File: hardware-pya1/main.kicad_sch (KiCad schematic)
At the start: 64 parts, among them J6 USB_C_Receptacle_USB2.0_16P, J7 Conn_02x08_Odd_Even, Q6 BSS138, SW1 SW_Push, SW10 SW_Push, SW11 SW_Push, SW12 SW_Push, SW13 SW_Push, SW14 SW_Push, SW15 SW_Push, SW16 SW_Push, SW17 SW_Push, SW18 SW_Push, SW19 SW_Push, SW2 SW_Push, SW20 SW_Push, SW21 Encoder, SW22 SW_Push, SW3 SW_Push, SW4 SW_Push, SW5 SW_Push, SW6 SW_Push, SW7 SW_Push, SW8 SW_Push, SW9 SW_Push, U3 74HC595, U4 ESP32-S3-WROOM-1

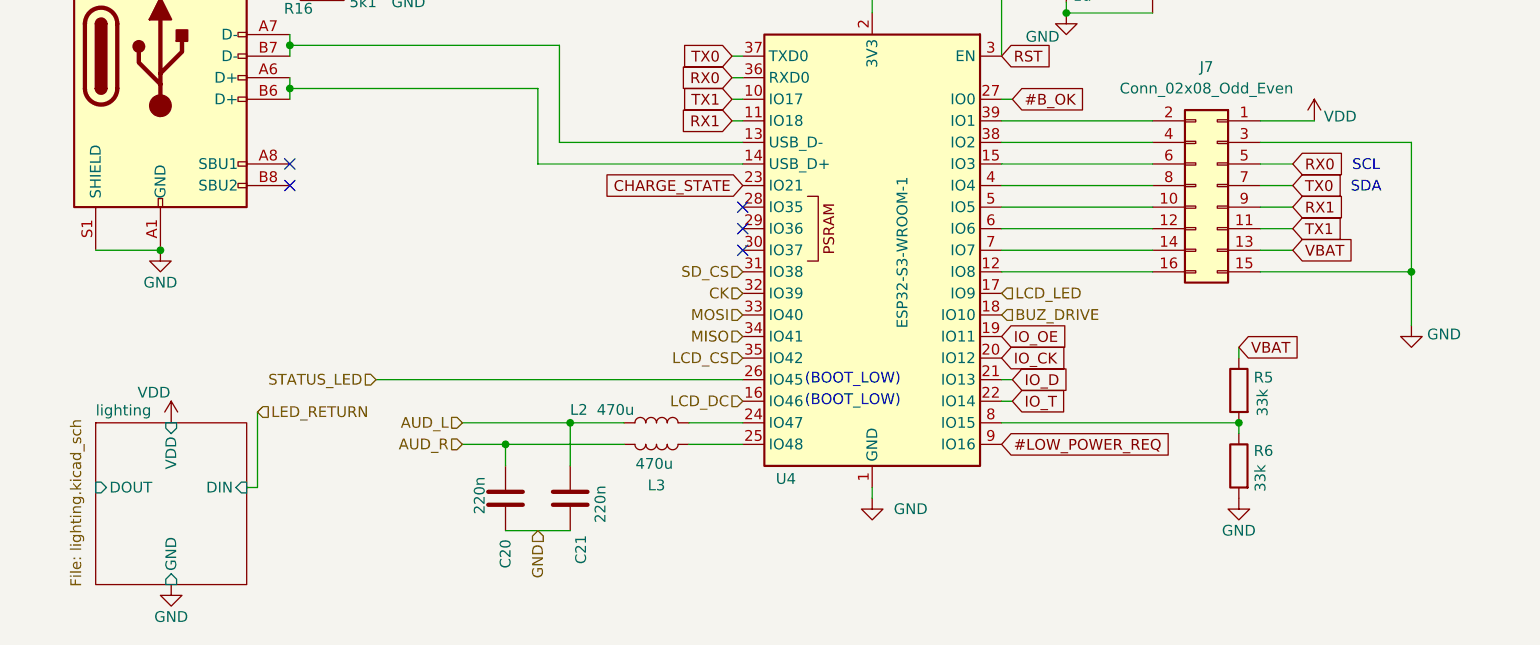
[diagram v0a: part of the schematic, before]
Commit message: pcb: redesign fix for LowPowerReq - added passives optional cap for slowstart on regulator switching to hi-power
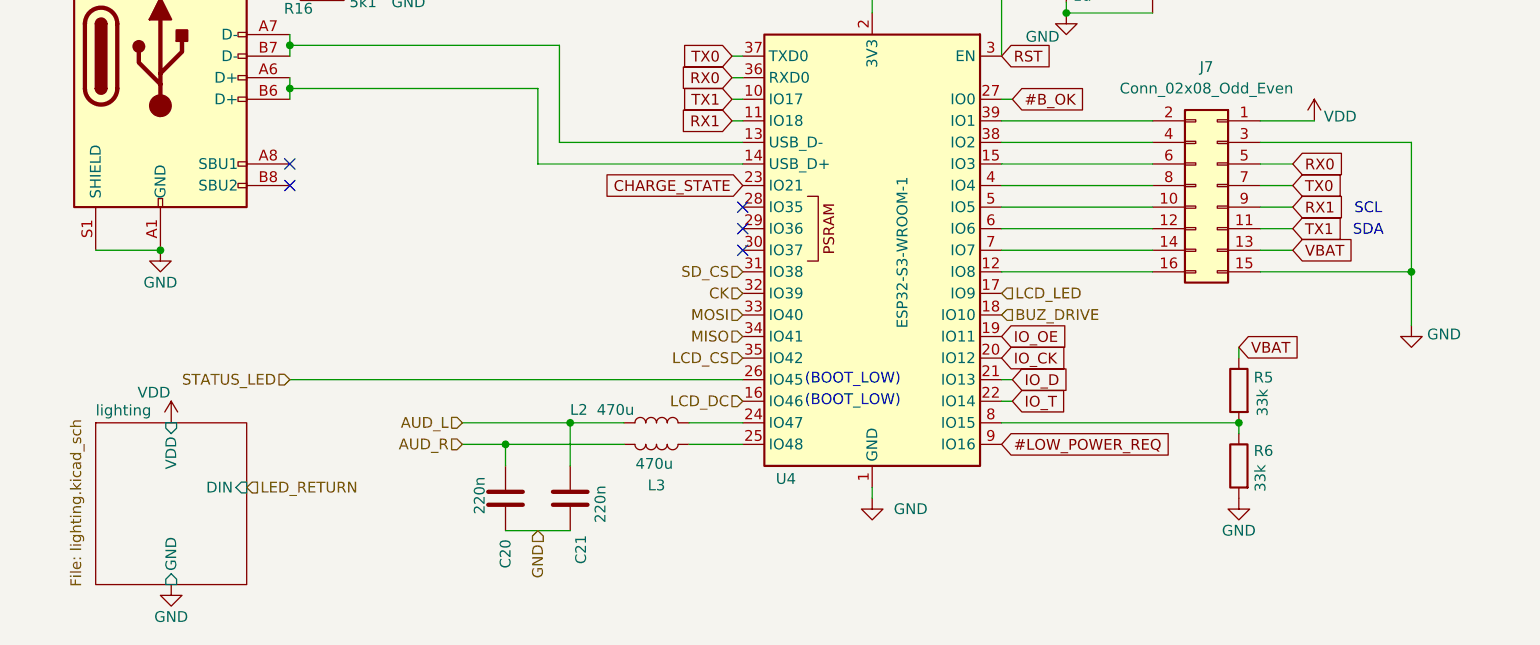
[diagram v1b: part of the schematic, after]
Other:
- sheet lighting ports: added none; removed DOUT
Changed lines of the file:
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@@
 	(wire
 		(pts
+			(xy 55.88 157.48) (xy 109.22 157.48)
+		)
+		(stroke
+			(width 0)
+			(type default)
+		)
+	)
+	(wire
+		(pts
 			(xy 57.15 63.5) (xy 77.47 63.5)
 		)
@@
 	(wire
 		(pts
-			(xy 52.07 161.29) (xy 52.07 170.18)
-		)
-		(stroke
-			(width 0)
-			(type default)
-		)
-	)
-	(wire
-		(pts
 			(xy 66.04 109.22) (xy 66.04 111.76)
 		)
@@
 	(wire
 		(pts
-			(xy 50.8 170.18) (xy 52.07 170.18)
-		)
-		(stroke
-			(width 0)
-			(type default)
-		)
-	)
-	(wire
-		(pts
 			(xy 232.41 57.15) (xy 229.87 57.15)
 		)
@@
 	(wire
 		(pts
-			(xy 66.04 157.48) (xy 109.22 157.48)
-		)
-		(stroke
-			(width 0)
-			(type default)
-		)
-	)
-	(wire
-		(pts
 			(xy 161.29 54.61) (xy 161.29 50.8)
 		)
@@
 	(text "SCL"
 		(exclude_from_sim no)
-		(at 182.626 132.334 0)
+		(at 182.88 137.414 0)
 		(effects
 			(font
@@
 	(text "SDA"
 		(exclude_from_sim no)
-		(at 182.626 134.874 0)
+		(at 182.88 139.954 0)
 		(effects
 			(font
@@
 	(hierarchical_label "STATUS_LED"
 		(shape input)
-		(at 66.04 157.48 180)
+		(at 55.88 157.48 180)
 		(effects
 			(font
@@
 		)
 	)
-	(hierarchical_label "LED_RETURN"
-		(shape input)
-		(at 52.07 161.29 0)
-		(effects
-			(font
-				(size 1.27 1.27)
-			)
-			(justify left)
-		)
-	)
 	(hierarchical_label "VDD"
 		(shape input)
@@
 		)
 	)
+	(hierarchical_label "LED_RETURN"
+		(shape input)
+		(at 50.8 170.18 0)
+		(effects
+			(font
+				(size 1.27 1.27)
+			)
+			(justify left)
+		)
+	)
 	(hierarchical_label "BUZ_DRIVE"
 		(shape input)
@@
 			)
 		)
-		(pin "DOUT" input
-			(at 33.02 170.18 180)
-			(effects
-				(font
-					(size 1.27 1.27)
-				)
-				(justify left)
-			)
-		)
